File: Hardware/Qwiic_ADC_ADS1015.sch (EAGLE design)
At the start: 23 parts, among them J4 Screw Pin Terminals, U1 ADS1015

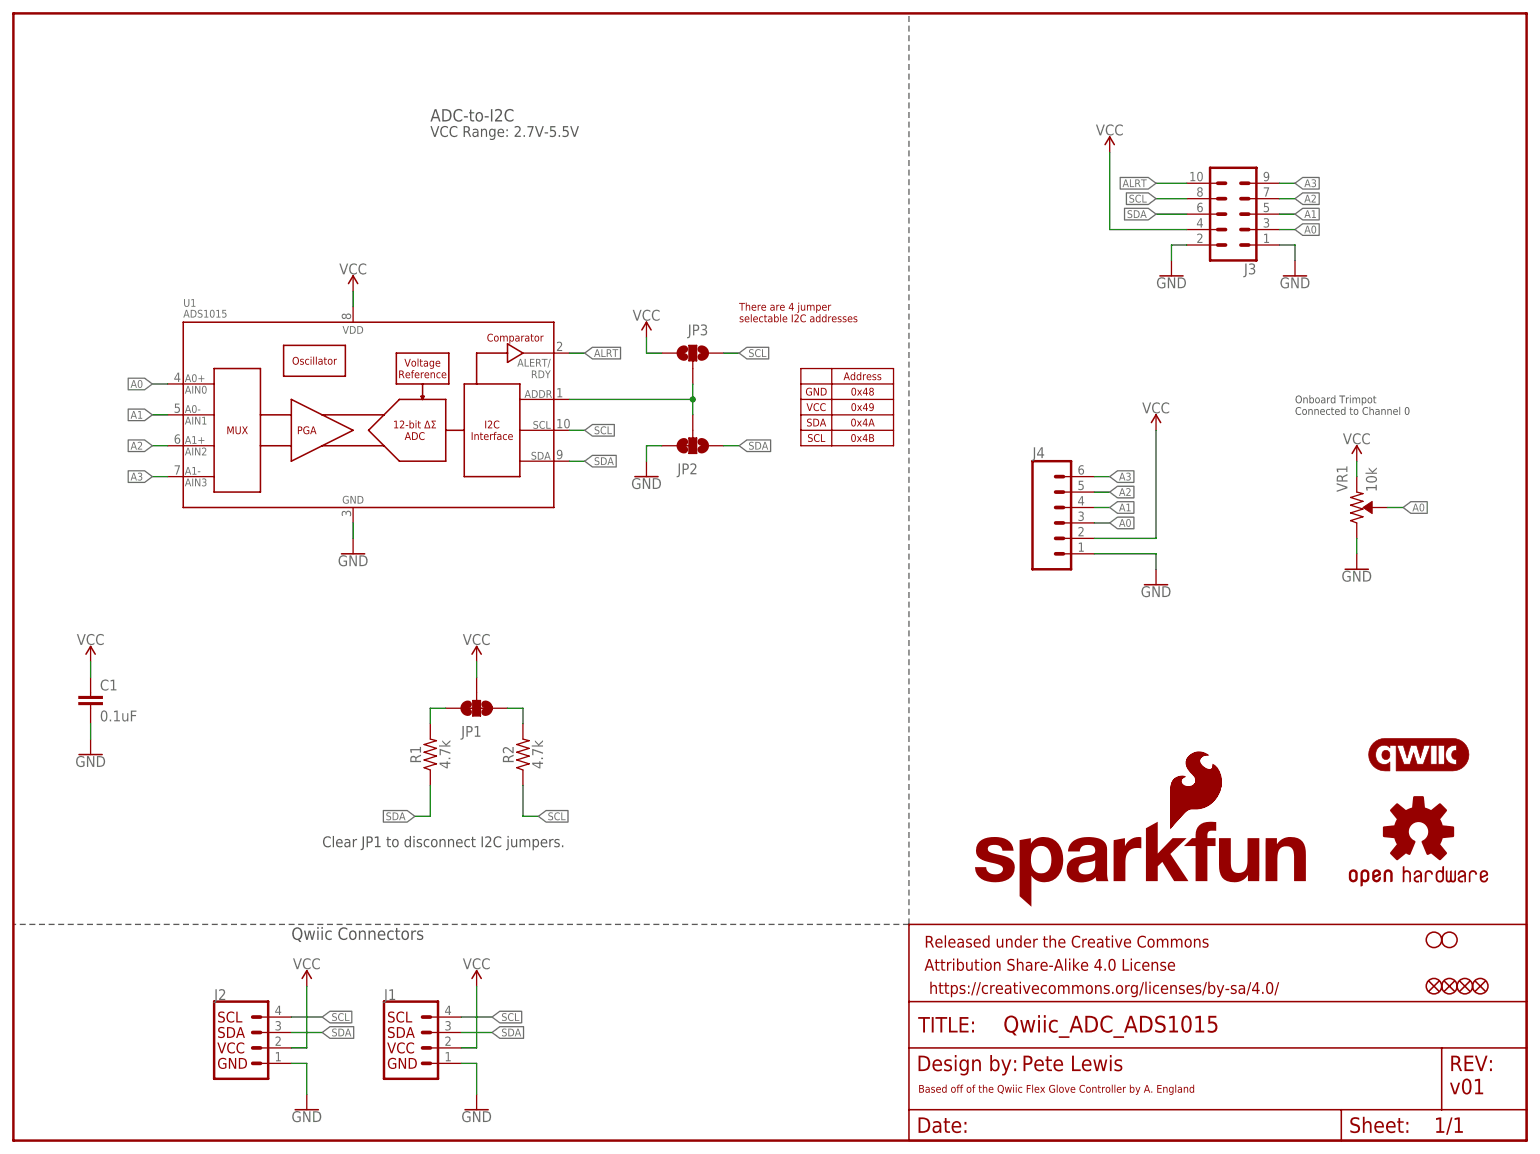
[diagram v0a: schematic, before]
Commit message: Hardware changes - pre-group review
JP4 label changed to TRIM A0, also labeled trimpot on tops the same.
Product name on bottom silk.
Flipped pin order to have GND on left side of standard I2C pinout.
Bottom labels now show differential inputs names (A0+, A0-, etc.)
Added power LED, moved OSHW logo to bottom silk.
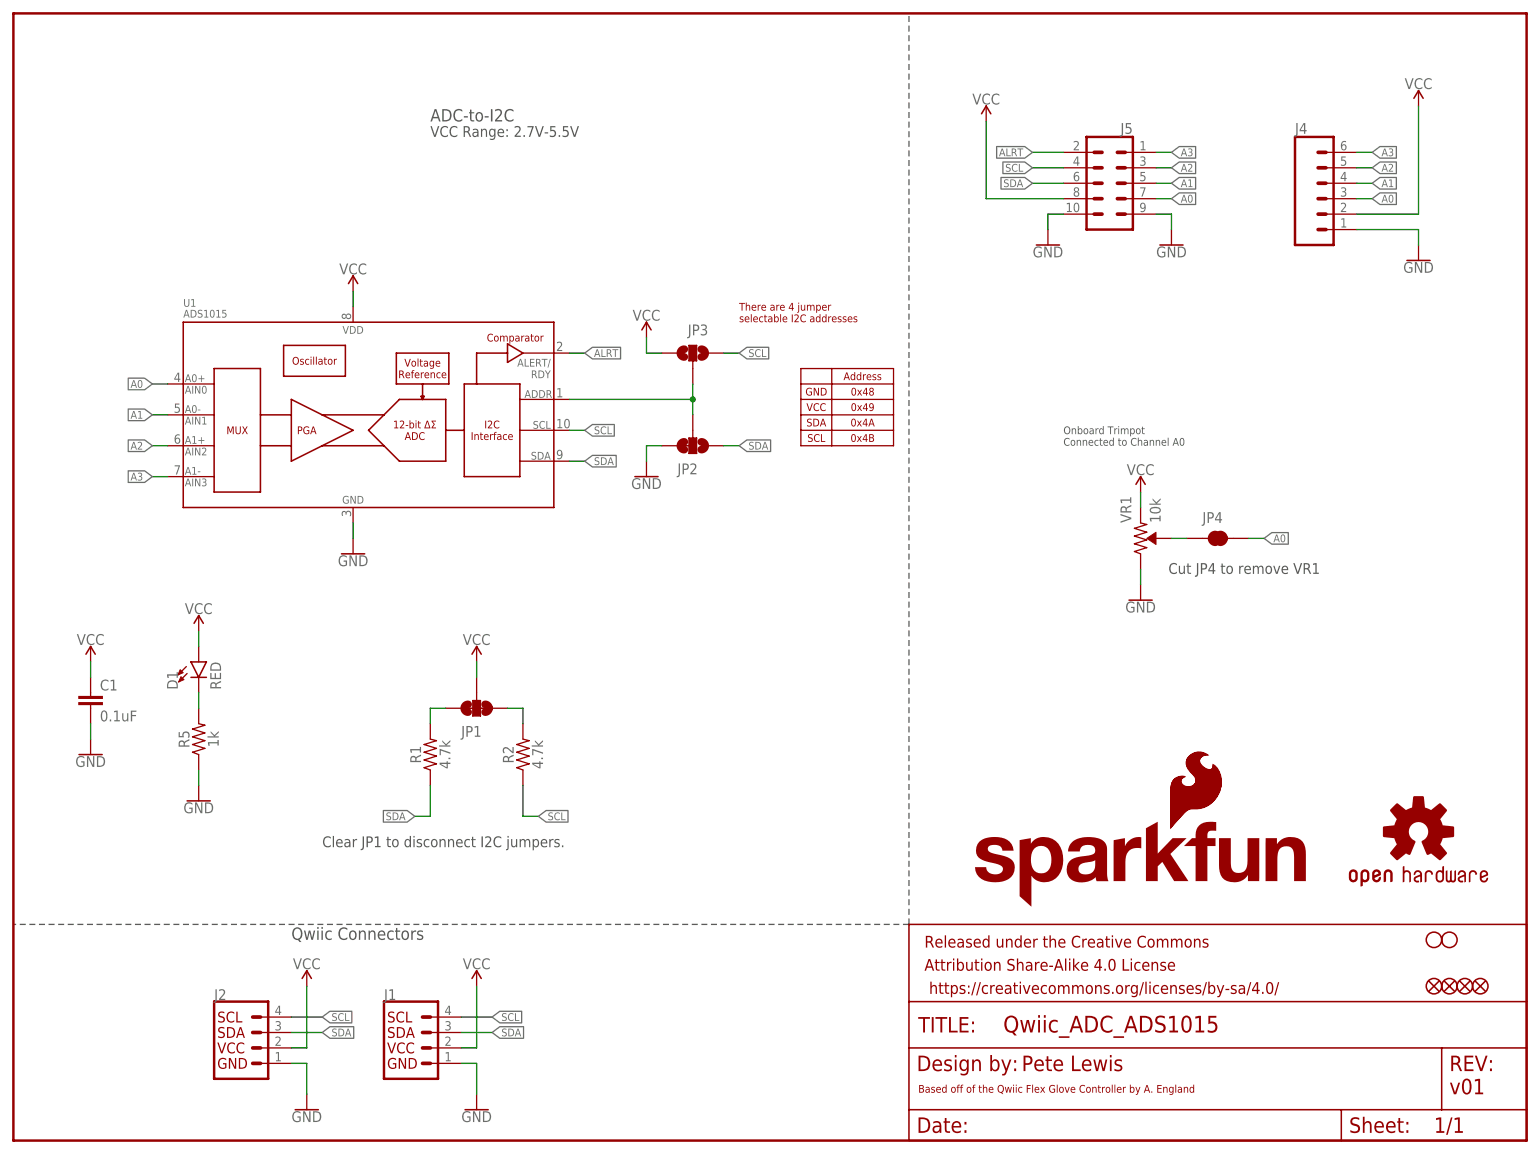
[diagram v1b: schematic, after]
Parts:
- removed J3: (no value), SparkFun-Connectors:CONN_05X2NO_SILK
- removed U$16: QWIIC_LOGO_5MM, SparkFun-Aesthetics:QWIIC_LOGO_5MM
- added D1: RED, SparkFun-LED:LED-RED0603
- added J5: (no value), SparkFun-Connectors:CONN_05X2NO_SILK
- added JP4: JUMPER-SMT_2_NC_TRACE_NO-SILK, SparkFun-Jumpers:JUMPER-SMT_2_NC_TRACE_NO-SILK
- added R5: 1k, SparkFun-Resistors:1KOHM-0603-1/10W-1%
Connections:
- new net N$1: JP4.1, VR1.WIPER
- new net N$2: D1.C, R5.2
- net A0: now also J5.7, JP4.2; no longer J3.3, VR1.WIPER
- net A1: now also J5.5; no longer J3.5
- net A2: now also J5.3; no longer J3.7
- net A3: now also J5.1; no longer J3.9
- net ALRT: now also J5.2; no longer J3.10
- net GND: now also J5.10, J5.9, R5.1; no longer J3.1, J3.2
- net SCL: now also J5.4; no longer J3.8
- net SDA: now also J5.6; no longer J3.6
- net VCC: now also D1.A, J5.8; no longer J3.4
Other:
- note added: "Cut JP4 to remove VR1"
- note added: "Onboard Trimpot Connected to Channel A0"
- note removed: "Onboard Trimpot Connected to Channel 0"
- moved on the sheet: J4, VR1

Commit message: updated product name silk
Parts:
- JP4: value JUMPER-SMT_2_NC_TRACE_NO-SILK -> JUMPER-SMT_2_NC_TRACE_SILK; device SparkFun-Jumpers:JUMPER-SMT_2_NC_TRACE_NO-SILK -> SparkFun-Jumpers:JUMPER-SMT_2_NC_TRACE_SILK
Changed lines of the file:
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@@
 <grid distance="0.1" unitdist="inch" unit="inch" style="lines" multiple="1" display="no" altdistance="0.01" altunitdist="inch" altunit="inch"/>
 <layers>
-<layer number="1" name="Top" color="4" fill="1" visible="no" active="no"/>
-<layer number="2" name="Route2" color="1" fill="3" visible="no" active="no"/>
-<layer number="3" name="Route3" color="4" fill="3" visible="no" active="no"/>
-<layer number="4" name="Route4" color="1" fill="4" visible="no" active="no"/>
-<layer number="5" name="Route5" color="4" fill="4" visible="no" active="no"/>
-<layer number="6" name="Route6" color="1" fill="8" visible="no" active="no"/>
-<layer number="7" name="Route7" color="4" fill="8" visible="no" active="no"/>
-<layer number="8" name="Route8" color="1" fill="2" visible="no" active="no"/>
-<layer number="9" name="Route9" color="4" fill="2" visible="no" active="no"/>
-<layer number="10" name="Route10" color="1" fill="7" visible="no" active="no"/>
-<layer number="11" name="Route11" color="4" fill="7" visible="no" active="no"/>
-<layer number="12" name="Route12" color="1" fill="5" visible="no" active="no"/>
-<layer number="13" name="Route13" color="4" fill="5" visible="no" active="no"/>
-<layer number="14" name="Route14" color="1" fill="6" visible="no" active="no"/>
-<layer number="15" name="Route15" color="4" fill="6" visible="no" active="no"/>
-<layer number="16" name="Bottom" color="1" fill="1" visible="no" active="no"/>
-<layer number="17" name="Pads" color="2" fill="1" visible="no" active="no"/>
-<layer number="18" name="Vias" color="2" fill="1" visible="no" active="no"/>
-<layer number="19" name="Unrouted" color="6" fill="1" visible="no" active="no"/>
-<layer number="20" name="Dimension" color="15" fill="1" visible="no" active="no"/>
-<layer number="21" name="tPlace" color="16" fill="1" visible="no" active="no"/>
-<layer number="22" name="bPlace" color="14" fill="1" visible="no" active="no"/>
-<layer number="23" name="tOrigins" color="15" fill="1" visible="no" active="no"/>
-<layer number="24" name="bOrigins" color="15" fill="1" visible="no" active="no"/>
-<layer number="25" name="tNames" color="7" fill="1" visible="no" active="no"/>
-<layer number="26" name="bNames" color="7" fill="1" visible="no" active="no"/>
-<layer number="27" name="tValues" color="7" fill="1" visible="no" active="no"/>
-<layer number="28" name="bValues" color="7" fill="1" visible="no" active="no"/>
+<layer number="1" name="Top" color="4" fill="1" visible="yes" active="no"/>
+<layer number="2" name="Route2" color="1" fill="3" visible="yes" active="no"/>
+<layer number="3" name="Route3" color="4" fill="3" visible="yes" active="no"/>
+<layer number="4" name="Route4" color="1" fill="4" visible="yes" active="no"/>
+<layer number="5" name="Route5" color="4" fill="4" visible="yes" active="no"/>
+<layer number="6" name="Route6" color="1" fill="8" visible="yes" active="no"/>
+<layer number="7" name="Route7" color="4" fill="8" visible="yes" active="no"/>
+<layer number="8" name="Route8" color="1" fill="2" visible="yes" active="no"/>
+<layer number="9" name="Route9" color="4" fill="2" visible="yes" active="no"/>
+<layer number="10" name="Route10" color="1" fill="7" visible="yes" active="no"/>
+<layer number="11" name="Route11" color="4" fill="7" visible="yes" active="no"/>
+<layer number="12" name="Route12" color="1" fill="5" visible="yes" active="no"/>
+<layer number="13" name="Route13" color="4" fill="5" visible="yes" active="no"/>
+<layer number="14" name="Route14" color="1" fill="6" visible="yes" active="no"/>
+<layer number="15" name="Route15" color="4" fill="6" visible="yes" active="no"/>
+<layer number="16" name="Bottom" color="1" fill="1" visible="yes" active="no"/>
+<layer number="17" name="Pads" color="2" fill="1" visible="yes" active="no"/>
+<layer number="18" name="Vias" color="2" fill="1" visible="yes" active="no"/>
+<layer number="19" name="Unrouted" color="6" fill="1" visible="yes" active="no"/>
+<layer number="20" name="Dimension" color="15" fill="1" visible="yes" active="no"/>
+<layer number="21" name="tPlace" color="16" fill="1" visible="yes" active="no"/>
+<layer number="22" name="bPlace" color="14" fill="1" visible="yes" active="no"/>
+<layer number="23" name="tOrigins" color="15" fill="1" visible="yes" active="no"/>
+<layer number="24" name="bOrigins" color="15" fill="1" visible="yes" active="no"/>
+<layer number="25" name="tNames" color="7" fill="1" visible="yes" active="no"/>
+<layer number="26" name="bNames" color="7" fill="1" visible="yes" active="no"/>
+<layer number="27" name="tValues" color="7" fill="1" visible="yes" active="no"/>
+<layer number="28" name="bValues" color="7" fill="1" visible="yes" active="no"/>
 <layer number="29" name="tStop" color="63" fill="3" visible="no" active="no"/>
 <layer number="30" name="bStop" color="7" fill="6" visible="no" active="no"/>
@@
 <layer number="35" name="tGlue" color="7" fill="4" visible="no" active="no"/>
 <layer number="36" name="bGlue" color="7" fill="5" visible="no" active="no"/>
-<layer number="37" name="tTest" color="7" fill="1" visible="no" active="no"/>
-<layer number="38" name="bTest" color="7" fill="1" visible="no" active="no"/>
+<layer number="37" name="tTest" color="7" fill="1" visible="yes" active="no"/>
+<layer number="38" name="bTest" color="7" fill="1" visible="yes" active="no"/>
 <layer number="39" name="tKeepout" color="4" fill="11" visible="no" active="no"/>
 <layer number="40" name="bKeepout" color="1" fill="11" visible="no" active="no"/>
@@
 <layer number="44" name="Drills" color="7" fill="1" visible="no" active="no"/>
 <layer number="45" name="Holes" color="7" fill="1" visible="no" active="no"/>
-<layer number="46" name="Milling" color="3" fill="1" visible="no" active="no"/>
-<layer number="47" name="Measures" color="7" fill="1" visible="no" active="no"/>
-<layer number="48" name="Document" color="7" fill="1" visible="no" active="no"/>
-<layer number="49" name="Reference" color="7" fill="1" visible="no" active="no"/>
-<layer number="50" name="dxf" color="7" fill="1" visible="no" active="no"/>
-<layer number="51" name="tDocu" color="6" fill="1" visible="no" active="no"/>
-<layer number="52" name="bDocu" color="7" fill="1" visible="no" active="no"/>
-<layer number="53" name="tGND_GNDA" color="7" fill="9" visible="no" active="no"/>
-<layer number="54" name="bGND_GNDA" color="1" fill="9" visible="no" active="no"/>
-<layer number="56" name="wert" color="7" fill="1" visible="no" active="no"/>
-<layer number="57" name="tCAD" color="7" fill="1" visible="no" active="no"/>
-<layer number="59" name="tCarbon" color="7" fill="1" visible="no" active="no"/>
-<layer number="60" name="bCarbon" color="7" fill="1" visible="no" active="no"/>
+<layer number="46" name="Milling" color="3" fill="1" visible="yes" active="no"/>
+<layer number="47" name="Measures" color="7" fill="1" visible="yes" active="no"/>
+<layer number="48" name="Document" color="7" fill="1" visible="yes" active="no"/>
+<layer number="49" name="Reference" color="7" fill="1" visible="yes" active="no"/>
+<layer number="50" name="dxf" color="7" fill="1" visible="yes" active="no"/>
+<layer number="51" name="tDocu" color="6" fill="1" visible="yes" active="no"/>
+<layer number="52" name="bDocu" color="7" fill="1" visible="yes" active="no"/>
+<layer number="53" name="tGND_GNDA" color="7" fill="9" visible="yes" active="no"/>
+<layer number="54" name="bGND_GNDA" color="1" fill="9" visible="yes" active="no"/>
+<layer number="56" name="wert" color="7" fill="1" visible="yes" active="no"/>
+<layer number="57" name="tCAD" color="7" fill="1" visible="yes" active="no"/>
+<layer number="59" name="tCarbon" color="7" fill="1" visible="yes" active="no"/>
+<layer number="60" name="bCarbon" color="7" fill="1" visible="yes" active="no"/>
 <layer number="88" name="SimResults" color="9" fill="1" visible="yes" active="yes"/>
 <layer number="89" name="SimProbes" color="9" fill="1" visible="yes" active="yes"/>
@@
 <part name="SUPPLY3" library="SparkFun-PowerSymbols" deviceset="VCC" device=""/>
 <part name="GND8" library="SparkFun-PowerSymbols" deviceset="GND" device=""/>
-<part name="JP4" library="SparkFun-Jumpers" deviceset="JUMPER-SMT_2_NC_TRACE" device="_NO-SILK" value=""/>
+<part name="JP4" library="SparkFun-Jumpers" deviceset="JUMPER-SMT_2_NC_TRACE" device="_SILK" value=""/>
 <part name="D1" library="SparkFun-LED" deviceset="LED-RED" device="0603" value="RED"/>
 <part name="R5" library="SparkFun-Resistors" deviceset="1KOHM" device="-0603-1/10W-1%" value="1k"/>
